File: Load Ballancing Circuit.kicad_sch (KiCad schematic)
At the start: 11 parts, among them J1 1757284, U1 LTC4359HMS8#PBF, U2 LTC4359HMS8#PBF

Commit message: Remove imported symbol table fields
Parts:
- C1, C2: @ QTY 1 -> (none); ALTIUM_VALUE 1500pF -> (none); MANUFACTURER Murata Electronics North America -> (none); MANUFACTURER PART NUMBER GRM216R71H152KA01D -> (none); Part Number (none) -> GRM216R71H152KA01D
- C3, C4: @ QTY 1 -> (none); ALTIUM_VALUE 330uF -> (none); MANUFACTURER Panasonic Electronic Components -> (none); MANUFACTURER PART NUMBER EEU-FM1V331LB -> (none); Part Number (none) -> EEU-FM1V331LB
- D1, D2: @ QTY 1 -> (none); ALTIUM_VALUE 26.7V -> (none); MANUFACTURER Littelfuse -> (none); MANUFACTURER PART NUMBER SMBJ24CA -> (none); Part Number (none) -> SMBJ24CA
- J1: @ QTY 1 -> (none); ALTIUM_VALUE 6 -> (none); MANUFACTURER Phoenix Contact -> (none); MANUFACTURER PART NUMBER 1757284 -> (none); Part Number (none) -> 1757284
- R1, R2: @ QTY 1 -> (none); ALTIUM_VALUE 1k -> (none); MANUFACTURER Panasonic Electronic Components -> (none); MANUFACTURER PART NUMBER ERJ-P06F1001V -> (none); Part Number (none) -> ERJ-P06F1001V
- U1, U2: @ QTY 1 -> (none); ALTIUM_VALUE N/A -> (none); MANUFACTURER Analog Devices -> (none); MANUFACTURER PART NUMBER LTC4359HMS8#PBF -> (none); Part Number (none) -> LTC4359HMS8#PBF
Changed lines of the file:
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@@
       (effects (font (size 1.27 1.27)) hide)
     )
-    (property "MANUFACTURER" "Phoenix Contact" (at 212.852 86.36 0)
-      (effects (font (size 1.27 1.27)) (justify left bottom) hide)
-    )
-    (property "MANUFACTURER PART NUMBER" "1757284" (at 212.852 86.36 0)
-      (effects (font (size 1.27 1.27)) (justify left bottom) hide)
-    )
-    (property "ALTIUM_VALUE" "6" (at 212.852 86.36 0)
-      (effects (font (size 1.27 1.27)) (justify left bottom) hide)
-    )
-    (property "@ QTY" "1" (at 212.852 86.36 0)
-      (effects (font (size 1.27 1.27)) (justify left bottom) hide)
+    (property "Part Number" "1757284" (at 213.36 91.44 0)
+      (effects (font (size 1.27 1.27)) hide)
     )
     (pin "1")
@@
       (effects (font (size 1.27 1.27)) hide)
     )
-    (property "MANUFACTURER" "Analog Devices" (at 60.452 40.64 0)
-      (effects (font (size 1.27 1.27)) (justify left bottom) hide)
-    )
-    (property "ALTIUM_VALUE" "N/A" (at 60.452 40.64 0)
-      (effects (font (size 1.27 1.27)) (justify left bottom) hide)
-    )
-    (property "MANUFACTURER PART NUMBER" "LTC4359HMS8#PBF" (at 60.452 40.64 0)
-      (effects (font (size 1.27 1.27)) (justify left bottom) hide)
-    )
-    (property "@ QTY" "1" (at 60.452 40.64 0)
-      (effects (font (size 1.27 1.27)) (justify left bottom) hide)
+    (property "Part Number" "LTC4359HMS8#PBF" (at 60.96 45.72 0)
+      (effects (font (size 1.27 1.27)) hide)
     )
     (pin "1")
@@
       (effects (font (size 1.27 1.27)) hide)
     )
-    (property "MANUFACTURER" "Panasonic Electronic Components" (at 30.226 47.752 0)
-      (effects (font (size 1.27 1.27)) (justify left bottom) hide)
-    )
-    (property "MANUFACTURER PART NUMBER" "EEU-FM1V331LB" (at 30.226 47.752 0)
-      (effects (font (size 1.27 1.27)) (justify left bottom) hide)
-    )
-    (property "ALTIUM_VALUE" "330uF" (at 30.226 47.752 0)
-      (effects (font (size 1.27 1.27)) (justify left bottom) hide)
-    )
-    (property "@ QTY" "1" (at 30.226 47.752 0)
-      (effects (font (size 1.27 1.27)) (justify left bottom) hide)
+    (property "Part Number" "EEU-FM1V331LB" (at 33.02 48.26 0)
+      (effects (font (size 1.27 1.27)) hide)
     )
     (pin "1")
@@
       (effects (font (size 1.27 1.27)) hide)
     )
-    (property "MANUFACTURER" "Murata Electronics North America" (at 110.236 118.11 0)
-      (effects (font (size 1.27 1.27)) (justify left bottom) hide)
-    )
-    (property "@ QTY" "1" (at 110.236 118.11 0)
-      (effects (font (size 1.27 1.27)) (justify left bottom) hide)
-    )
-    (property "ALTIUM_VALUE" "1500pF" (at 110.236 118.11 0)
-      (effects (font (size 1.27 1.27)) (justify left bottom) hide)
-    )
-    (property "MANUFACTURER PART NUMBER" "GRM216R71H152KA01D" (at 110.236 118.872 0)
-      (effects (font (size 1.27 1.27)) (justify left bottom) hide)
+    (property "Part Number" "GRM216R71H152KA01D" (at 111.76 121.92 0)
+      (effects (font (size 1.27 1.27)) hide)
     )
     (pin "1")
@@
       (effects (font (size 1.27 1.27)) hide)
     )
-    (property "MANUFACTURER" "Murata Electronics North America" (at 110.236 54.61 0)
-      (effects (font (size 1.27 1.27)) (justify left bottom) hide)
-    )
-    (property "@ QTY" "1" (at 110.236 54.61 0)
-      (effects (font (size 1.27 1.27)) (justify left bottom) hide)
-    )
-    (property "ALTIUM_VALUE" "1500pF" (at 110.236 54.61 0)
-      (effects (font (size 1.27 1.27)) (justify left bottom) hide)
-    )
-    (property "MANUFACTURER PART NUMBER" "GRM216R71H152KA01D" (at 110.236 55.372 0)
-      (effects (font (size 1.27 1.27)) (justify left bottom) hide)
+    (property "Part Number" "GRM216R71H152KA01D" (at 111.76 58.42 0)
+      (effects (font (size 1.27 1.27)) hide)
     )
     (pin "1")
@@
       (effects (font (size 1.27 1.27)) hide)
     )
-    (property "MANUFACTURER" "Panasonic Electronic Components" (at 116.332 135.89 0)
-      (effects (font (size 1.27 1.27)) (justify left bottom) hide)
-    )
-    (property "@ QTY" "1" (at 116.332 135.89 0)
-      (effects (font (size 1.27 1.27)) (justify left bottom) hide)
-    )
-    (property "ALTIUM_VALUE" "1k" (at 116.332 135.89 0)
-      (effects (font (size 1.27 1.27)) (justify left bottom) hide)
-    )
-    (property "MANUFACTURER PART NUMBER" "ERJ-P06F1001V" (at 116.332 138.684 0)
-      (effects (font (size 1.27 1.27)) (justify left bottom) hide)
+    (property "Part Number" "ERJ-P06F1001V" (at 121.92 139.7 0)
+      (effects (font (size 1.27 1.27)) hide)
     )
     (pin "1")
@@
       (effects (font (size 1.27 1.27)) hide)
     )
-    (property "MANUFACTURER" "Littelfuse" (at 42.926 47.752 0)
-      (effects (font (size 1.27 1.27)) (justify left bottom) hide)
-    )
-    (property "MANUFACTURER PART NUMBER" "SMBJ24CA" (at 42.926 47.752 0)
-      (effects (font (size 1.27 1.27)) (justify left bottom) hide)
-    )
-    (property "ALTIUM_VALUE" "26.7V" (at 42.926 50.292 0)
-      (effects (font (size 1.27 1.27)) (justify left bottom) hide)
-    )
-    (property "@ QTY" "1" (at 42.926 50.292 0)
-      (effects (font (size 1.27 1.27)) (justify left bottom) hide)
+    (property "Part Number" "SMBJ24CA" (at 45.72 63.5 0)
+      (effects (font (size 1.27 1.27)) hide)
     )
     (pin "A")
@@
       (effects (font (size 1.27 1.27)) hide)
     )
-    (property "MANUFACTURER" "Panasonic Electronic Components" (at 30.226 111.252 0)
-      (effects (font (size 1.27 1.27)) (justify left bottom) hide)
-    )
-    (property "MANUFACTURER PART NUMBER" "EEU-FM1V331LB" (at 30.226 111.252 0)
-      (effects (font (size 1.27 1.27)) (justify left bottom) hide)
-    )
-    (property "ALTIUM_VALUE" "330uF" (at 30.226 111.252 0)
-      (effects (font (size 1.27 1.27)) (justify left bottom) hide)
-    )
-    (property "@ QTY" "1" (at 30.226 111.252 0)
-      (effects (font (size 1.27 1.27)) (justify left bottom) hide)
+    (property "Part Number" "EEU-FM1V331LB" (at 33.02 111.76 0)
+      (effects (font (size 1.27 1.27)) hide)
     )
     (pin "1")
@@
       (effects (font (size 1.27 1.27)) hide)
     )
-    (property "MANUFACTURER" "Littelfuse" (at 42.926 111.252 0)
-      (effects (font (size 1.27 1.27)) (justify left bottom) hide)
-    )
-    (property "MANUFACTURER PART NUMBER" "SMBJ24CA" (at 42.926 111.252 0)
-      (effects (font (size 1.27 1.27)) (justify left bottom) hide)
-    )
-    (property "ALTIUM_VALUE" "26.7V" (at 42.926 113.792 0)
-      (effects (font (size 1.27 1.27)) (justify left bottom) hide)
-    )
-    (property "@ QTY" "1" (at 42.926 113.792 0)
-      (effects (font (size 1.27 1.27)) (justify left bottom) hide)
+    (property "Part Number" "SMBJ24CA" (at 45.72 127 0)
+      (effects (font (size 1.27 1.27)) hide)
     )
     (pin "A")
@@
       (effects (font (size 1.27 1.27)) hide)
     )
-    (property "MANUFACTURER" "Analog Devices" (at 60.452 104.14 0)
-      (effects (font (size 1.27 1.27)) (justify left bottom) hide)
-    )
-    (property "ALTIUM_VALUE" "N/A" (at 60.452 104.14 0)
-      (effects (font (size 1.27 1.27)) (justify left bottom) hide)
-    )
-    (property "MANUFACTURER PART NUMBER" "LTC4359HMS8#PBF" (at 60.452 104.14 0)
-      (effects (font (size 1.27 1.27)) (justify left bottom) hide)
-    )
-    (property "@ QTY" "1" (at 60.452 104.14 0)
-      (effects (font (size 1.27 1.27)) (justify left bottom) hide)
+    (property "Part Number" "LTC4359HMS8#PBF" (at 60.96 109.22 0)
+      (effects (font (size 1.27 1.27)) hide)
     )
     (pin "1")
@@
       (effects (font (size 1.27 1.27)) hide)
     )
-    (property "MANUFACTURER" "Panasonic Electronic Components" (at 116.332 72.39 0)
-      (effects (font (size 1.27 1.27)) (justify left bottom) hide)
-    )
-    (property "@ QTY" "1" (at 116.332 72.39 0)
-      (effects (font (size 1.27 1.27)) (justify left bottom) hide)
-    )
-    (property "ALTIUM_VALUE" "1k" (at 116.332 72.39 0)
-      (effects (font (size 1.27 1.27)) (justify left bottom) hide)
-    )
-    (property "MANUFACTURER PART NUMBER" "ERJ-P06F1001V" (at 116.332 75.184 0)
-      (effects (font (size 1.27 1.27)) (justify left bottom) hide)
-    )
-    (pin "1")
+    (property "Part Number" "ERJ-P06F1001V" (at 121.92 76.2 0)
+      (effects (font (size 1.27 1.27)) hide)
+    )
+    (pin "1")

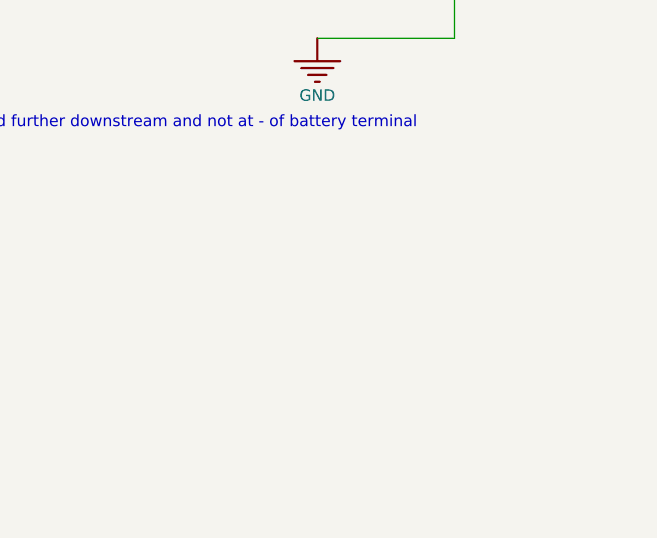
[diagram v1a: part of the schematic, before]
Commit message: V and I Monitoring Module
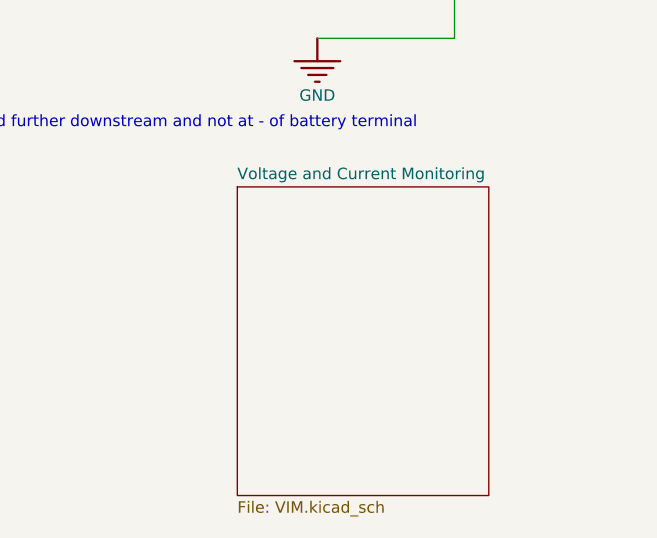
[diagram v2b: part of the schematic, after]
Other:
- added sheet Voltage and Current Monitoring (VIM.kicad_sch)
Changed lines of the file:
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@@
+    )
+  )
+  (sheet (at 184.15 135.89) (size 27.94 34.29) (fields_autoplaced)
+    (stroke (width 0.1524) (type solid))
+    (fill (color 0 0 0 0.0000))
+    (property "Sheetname" "Voltage and Current Monitoring" (at 184.15 135.1784 0)
+      (effects (font (size 1.27 1.27)) (justify left bottom))
+    )
+    (property "Sheetfile" "VIM.kicad_sch" (at 184.15 170.7646 0)
+      (effects (font (size 1.27 1.27)) (justify left top))
+    )
+    (instances
+      (project "Load Ballancing Circuit"
+        (path "/3c80be29-1084-4d09-9b70-344866d482c5" (page "1"))
+      )
     )
   )

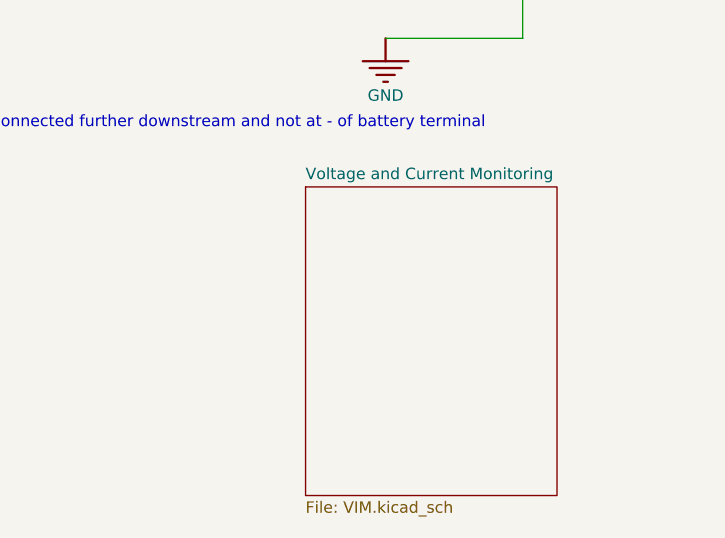
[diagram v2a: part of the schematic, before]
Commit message: Added some ports
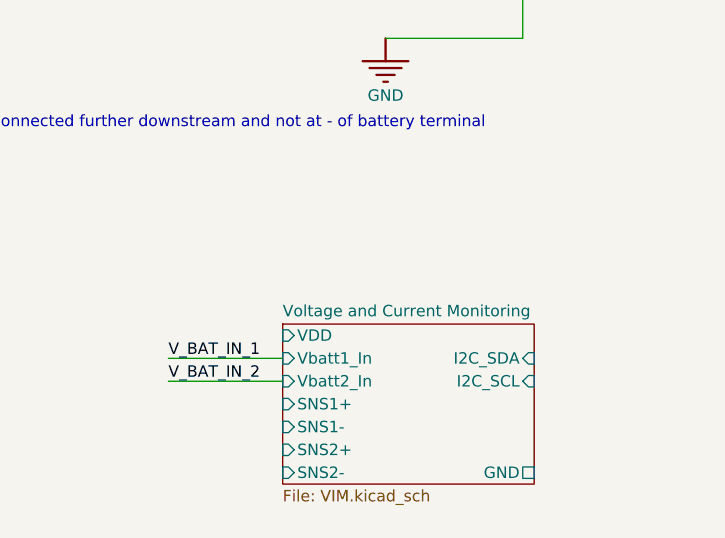
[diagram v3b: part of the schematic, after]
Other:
- sheet Voltage and Current Monitoring ports: added GND, I2C_SCL, I2C_SDA, SNS1+, SNS1-, SNS2+, SNS2-, VDD, Vbatt1_In, Vbatt2_In; removed none
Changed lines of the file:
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@@
     (stroke (width 0.254) (type default))
+  )
+  (wire (pts (xy 168.91 157.48) (xy 181.61 157.48))
+    (stroke (width 0) (type default))
   )
   (wire (pts (xy 132.08 139.7) (xy 132.08 144.78))
@@
   (wire (pts (xy 55.88 114.3) (xy 60.96 114.3))
     (stroke (width 0.254) (type default))
+  )
+  (wire (pts (xy 168.91 154.94) (xy 181.61 154.94))
+    (stroke (width 0) (type default))
   )
   (wire (pts (xy 101.6 45.72) (xy 114.3 45.72))
@@
     (effects (font (size 1.27 1.27)) (justify left bottom))
   )
+  (label "V_BAT_IN_2" (at 168.91 157.48 0) (fields_autoplaced)
+    (effects (font (size 1.27 1.27)) (justify left bottom))
+  )
   (label "V_BAT_OUT" (at 144.286 55.88 0) (fields_autoplaced)
+    (effects (font (size 1.27 1.27)) (justify left bottom))
+  )
+  (label "V_BAT_IN_1" (at 168.91 154.94 0) (fields_autoplaced)
     (effects (font (size 1.27 1.27)) (justify left bottom))
   )
@@
     )
   )
-  (sheet (at 184.15 135.89) (size 27.94 34.29) (fields_autoplaced)
+  (sheet (at 181.61 151.13) (size 27.94 17.78) (fields_autoplaced)
     (stroke (width 0.1524) (type solid))
     (fill (color 0 0 0 0.0000))
-    (property "Sheetname" "Voltage and Current Monitoring" (at 184.15 135.1784 0)
-      (effects (font (size 1.27 1.27)) (justify left bottom))
-    )
-    (property "Sheetfile" "VIM.kicad_sch" (at 184.15 170.7646 0)
+    (property "Sheetname" "Voltage and Current Monitoring" (at 181.61 150.4184 0)
+      (effects (font (size 1.27 1.27)) (justify left bottom))
+    )
+    (property "Sheetfile" "VIM.kicad_sch" (at 181.61 169.4946 0)
       (effects (font (size 1.27 1.27)) (justify left top))
     )
-    (instances
+    (pin "SNS2+" input (at 181.61 165.1 180)
+      (effects (font (size 1.27 1.27)) (justify left))
+    )
+    (pin "SNS2-" input (at 181.61 167.64 180)
+      (effects (font (size 1.27 1.27)) (justify left))
+    )
+    (pin "Vbatt1_In" input (at 181.61 154.94 180)
+      (effects (font (size 1.27 1.27)) (justify left))
+    )
+    (pin "Vbatt2_In" input (at 181.61 157.48 180)
+      (effects (font (size 1.27 1.27)) (justify left))
+    )
+    (pin "I2C_SDA" input (at 209.55 154.94 0)
+      (effects (font (size 1.27 1.27)) (justify right))
+    )
+    (pin "I2C_SCL" input (at 209.55 157.48 0)
+      (effects (font (size 1.27 1.27)) (justify right))
+    )
+    (pin "SNS1+" input (at 181.61 160.02 180)
+      (effects (font (size 1.27 1.27)) (justify left))
+    )
+    (pin "SNS1-" input (at 181.61 162.56 180)
+      (effects (font (size 1.27 1.27)) (justify left))
+    )
+    (pin "VDD" input (at 181.61 152.4 180)
+      (effects (font (size 1.27 1.27)) (justify left))
+    )
+    (pin "GND" passive (at 209.55 167.64 0)
+      (effects (font (size 1.27 1.27)) (justify right))
+    )
+    (instances

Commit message: added connectors and did layout
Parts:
- removed J1: 1757284, AltiumImport:SHDRRA6W100P0X508_1X6_3240X1200X860P, symbol Load Ballancing Circuit-altium-import:root_0_1757284
- added J2: 171857-0005, KK254:1718570005, symbol kk254-headers:171857-0005
- added J3: 171857-0004, KK254:1718570004, symbol kk254-headers:171857-0004
- added J4: 171857-0006, KK254:1718570006, symbol kk254-headers:171857-0006
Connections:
- net GATE_1: now also J4.2
- net GATE_2: now also J4.4
- net GND: now also J3.2, J4.6
- net V_BAT_IN_1: now also J4.1
- net V_BAT_IN_2: now also J4.3
- net V_BAT_OUT: now also J4.5
- new net 3V3: J2.1, J3.1
- new net I2C_SCL: J3.4
- new net I2C_SDA: J3.3
- new net SNS1+: J2.2
- new net SNS1-: J2.3
- new net SNS2+: J2.4
- new net SNS2-: J2.5
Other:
- note added: "I2C Header"
